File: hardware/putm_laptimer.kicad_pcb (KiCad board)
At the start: 4 copper layers, 76 x 75 mm, 48 parts, among them J1 Conn_01x22, J10 Conn_01x07, J11 Conn_01x09, J12 Conn_01x01, J13 Conn_01x01, J14 Conn_01x01, J15 Conn_01x01, J2 Conn_01x22, J3 Conn_01x22, J4 Conn_01x22, J5 M80-5001805, J6 Conn_02x05_Odd_Even, J7 734-163, J8 734-162, J9 Conn_01x07

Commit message: Increased buck converter pin hole diameter
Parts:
- J12, J13, J14, J15: footprint TestPoint:TestPoint_THTPad_D1.5mm_Drill0.7mm -> TestPoint:TestPoint_THTPad_D2.0mm_Drill1.0mm
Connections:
- net /IO13_GATE2 renamed /IO13
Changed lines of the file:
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@@
 	(net 18 "/IO19_PIN")
 	(net 19 "/IO14_GATE1")
-	(net 20 "/IO13_GATE2")
+	(net 20 "/IO13")
 	(net 21 "/IO37_PIN")
 	(net 22 "/IO35_PIN")
@@
 			(layers "*.Cu" "*.Mask")
 			(remove_unused_layers no)
-			(net 20 "/IO13_GATE2")
+			(net 20 "/IO13")
 			(pinfunction "Pin_19")
 			(pintype "passive")
@@
 		)
 	)
-	(footprint "TestPoint:TestPoint_THTPad_D1.5mm_Drill0.7mm"
+	(footprint "TestPoint:TestPoint_THTPad_D2.0mm_Drill1.0mm"
 		(layer "F.Cu")
 		(at 133.96 91.5 90)
-		(descr "THT pad as test Point, diameter 1.5mm, hole diameter 0.7mm")
+		(descr "THT pad as test Point, diameter 2.0mm, hole diameter 1.0mm")
 		(tags "test point THT pad")
 		(property "Reference" "J14"
-			(at 4 0.124695 90)
+			(at 3 0.04 180)
 			(layer "F.SilkS")
 			(effects
 				(font
-					(size 1 1)
+					(size 0.7 0.7)
 					(thickness 0.15)
 				)
@@
 		)
 		(property "Value" "Conn_01x01"
-			(at 0 1.75 90)
+			(at 0 2.05 90)
 			(layer "F.Fab")
 			(effects
@@
 		(fp_circle
 			(center 0 0)
-			(end 0 0.95)
+			(end 0 1.2)
 			(stroke
 				(width 0.12)
@@
 		(fp_circle
 			(center 0 0)
-			(end 1.25 0)
+			(end 1.5 0)
 			(stroke
 				(width 0.05)
@@
 		)
 		(fp_text user "${REFERENCE}"
-			(at 0 -1.65 90)
+			(at 0 -2 90)
 			(layer "F.Fab")
 			(effects
@@
 		(pad "1" thru_hole circle
 			(at 0 0 90)
-			(size 1.5 1.5)
-			(drill 0.7)
+			(size 2 2)
+			(drill 1)
 			(layers "*.Cu" "*.Mask")
 			(remove_unused_layers no)
@@
 		(embedded_fonts no)
 	)
-	(footprint "TestPoint:TestPoint_THTPad_D1.5mm_Drill0.7mm"
+	(footprint "TestPoint:TestPoint_THTPad_D2.0mm_Drill1.0mm"
 		(layer "F.Cu")
 		(at 136.5 91.5 90)
-		(descr "THT pad as test Point, diameter 1.5mm, hole diameter 0.7mm")
+		(descr "THT pad as test Point, diameter 2.0mm, hole diameter 1.0mm")
 		(tags "test point THT pad")
 		(property "Reference" "J15"
-			(at 4 0.084695 90)
+			(at 3 0 180)
 			(layer "F.SilkS")
 			(effects
 				(font
-					(size 1 1)
+					(size 0.7 0.7)
 					(thickness 0.15)
 				)
@@
 		)
 		(property "Value" "Conn_01x01"
-			(at 0 1.75 90)
+			(at 0 2.05 90)
 			(layer "F.Fab")
 			(effects
@@
 		(fp_circle
 			(center 0 0)
-			(end 0 0.95)
+			(end 0 1.2)
 			(stroke
 				(width 0.12)
@@
 		(fp_circle
 			(center 0 0)
-			(end 1.25 0)
+			(end 1.5 0)
 			(stroke
 				(width 0.05)
@@
 		)
 		(fp_text user "${REFERENCE}"
-			(at 0 -1.65 90)
+			(at 0 -2 90)
 			(layer "F.Fab")
 			(effects
@@
 		(pad "1" thru_hole circle
 			(at 0 0 90)
-			(size 1.5 1.5)
-			(drill 0.7)
+			(size 2 2)
+			(drill 1)
 			(layers "*.Cu" "*.Mask")
 			(remove_unused_layers no)
@@
 		)
 	)
-	(footprint "TestPoint:TestPoint_THTPad_D1.5mm_Drill0.7mm"
+	(footprint "TestPoint:TestPoint_THTPad_D2.0mm_Drill1.0mm"
 		(layer "F.Cu")
 		(at 128.88 91.5 90)
-		(descr "THT pad as test Point, diameter 1.5mm, hole diameter 0.7mm")
+		(descr "THT pad as test Point, diameter 2.0mm, hole diameter 1.0mm")
 		(tags "test point THT pad")
 		(property "Reference" "J12"
-			(at 4 0.08 90)
+			(at 3 0.06 180)
 			(layer "F.SilkS")
 			(effects
 				(font
-					(size 1 1)
+					(size 0.7 0.7)
 					(thickness 0.15)
 				)
@@
 		)
 		(property "Value" "Conn_01x01"
-			(at 0 1.75 90)
+			(at 0 2.05 90)
 			(layer "F.Fab")
 			(effects
@@
 		(fp_circle
 			(center 0 0)
-			(end 0 0.95)
+			(end 0 1.2)
 			(stroke
 				(width 0.12)
@@
 		(fp_circle
 			(center 0 0)
-			(end 1.25 0)
+			(end 1.5 0)
 			(stroke
 				(width 0.05)
@@
 		)
 		(fp_text user "${REFERENCE}"
-			(at 0 -1.65 90)
+			(at 0 -2 90)
 			(layer "F.Fab")
 			(effects
@@
 		(pad "1" thru_hole circle
 			(at 0 0 90)
-			(size 1.5 1.5)
-			(drill 0.7)
+			(size 2 2)
+			(drill 1)
 			(layers "*.Cu" "*.Mask")
 			(remove_unused_layers no)
@@
 			(layers "*.Cu" "*.Mask")
 			(remove_unused_layers no)
-			(net 20 "/IO13_GATE2")
+			(net 20 "/IO13")
 			(pinfunction "Pin_19")
 			(pintype "passive")
@@
 			)
 		)
-		(property "Datasheet" "734-162"
+		(property "Datasheet" "https://www.wago.com/pl/wielowtyki/wtyk-tht/p/734-162#details"
 			(at 0 0 0)
 			(layer "F.Fab")
@@
 		)
 	)
-	(footprint "TestPoint:TestPoint_THTPad_D1.5mm_Drill0.7mm"
+	(footprint "TestPoint:TestPoint_THTPad_D2.0mm_Drill1.0mm"
 		(layer "F.Cu")
 		(at 131.42 91.5 90)
-		(descr "THT pad as test Point, diameter 1.5mm, hole diameter 0.7mm")
+		(descr "THT pad as test Point, diameter 2.0mm, hole diameter 1.0mm")
 		(tags "test point THT pad")
 		(property "Reference" "J13"
-			(at 4 0 90)
+			(at 3 0.08 180)
 			(layer "F.SilkS")
 			(effects
 				(font
-					(size 1 1)
+					(size 0.7 0.7)
 					(thickness 0.15)
 				)
@@
 		)
 		(property "Value" "Conn_01x01"
-			(at 0 1.75 90)
+			(at 0 2.05 90)
 			(layer "F.Fab")
 			(effects
@@
 		(fp_circle
 			(center 0 0)
-			(end 0 0.95)
+			(end 0 1.2)
 			(stroke
 				(width 0.12)
@@
 		(fp_circle
 			(center 0 0)
-			(end 1.25 0)
+			(end 1.5 0)
 			(stroke
 				(width 0.05)
@@
 		)
 		(fp_text user "${REFERENCE}"
-			(at 0 -1.65 90)
+			(at 0 -2 90)
 			(layer "F.Fab")
 			(effects
@@
 		(pad "1" thru_hole circle
 			(at 0 0 90)
-			(size 1.5 1.5)
-			(drill 0.7)
+			(size 2 2)
+			(drill 1)
 			(layers "*.Cu" "*.Mask")
 			(remove_unused_layers no)
@@
 			)
 		)
-		(property "Datasheet" "734-163"
+		(property "Datasheet" "https://www.wago.com/pl/wielowtyki/wtyk-tht/p/734-163#details"
 			(at 0 0 0)
 			(layer "F.Fab")

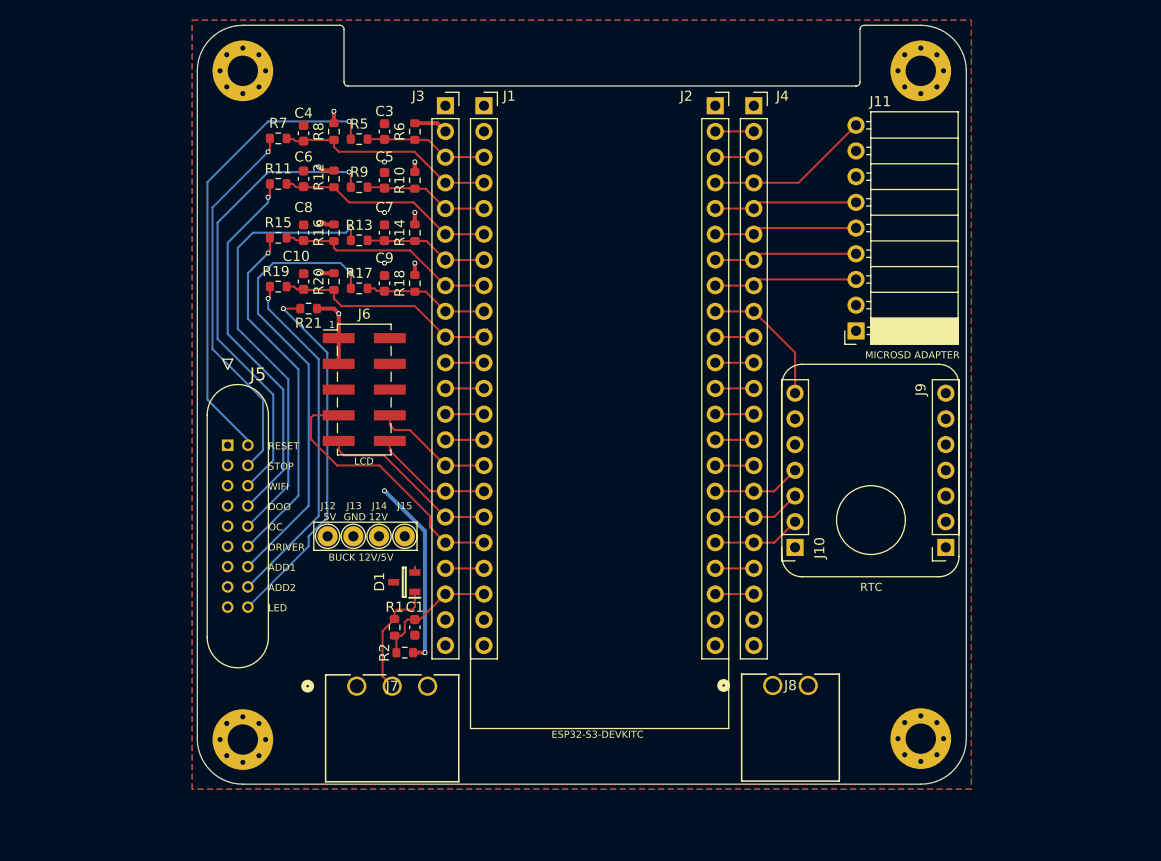
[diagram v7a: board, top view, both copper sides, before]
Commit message: Changed connectors
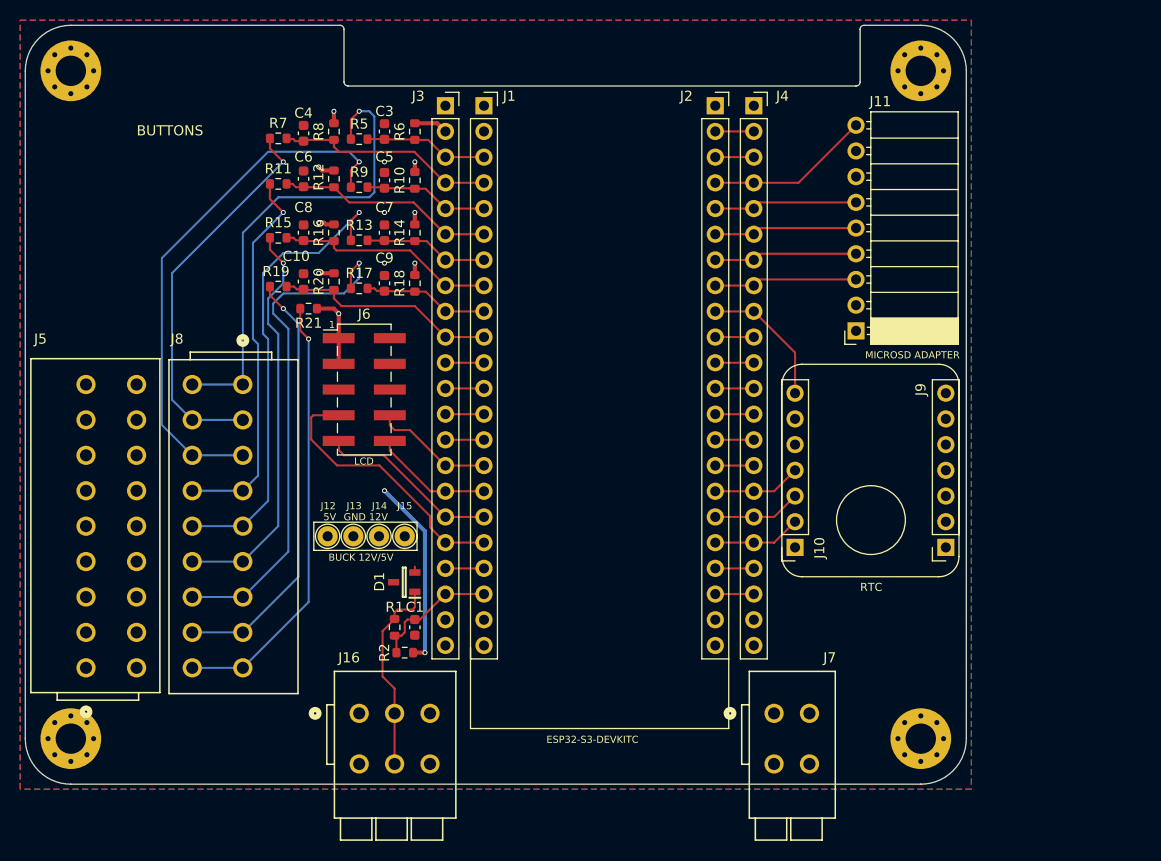
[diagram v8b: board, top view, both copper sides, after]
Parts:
- added J16: 2601-1103, Footprint:CONN3_2601-1103_WAG, F.Cu at (132.0, 109.0)
- J5: value M80-5001805 -> 2601-3109; footprint Footprint:M80-50018YY_2 -> Footprint:CONN9_2601-3109_WAG
- J7: value 734-163 -> 2601-1102; footprint Footprint:CONN3_734-163_WAG -> Footprint:CONN2_2601-1102_WAG
- J8: value 734-162 -> 2601-3109; footprint Footprint:CONN2_734-162_WAG -> Footprint:CONN9_2601-3109_WAG
- moved J8 60.2 mm to (120.5, 76.5), turned to -90 degrees
- moved J7 41.3 mm to (173.0, 109.0)
- moved J5 26.1 mm to (105.0, 104.5), turned to 90 degrees
- moved REF** 17.0 mm to (103.5, 111.5)
- moved REF** 17.0 mm to (103.5, 45.5)
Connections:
- D1 pad 1: Net-(D1-Pad1) -> Net-(J16-2_1)
- J5 pad 10: /RST_BTN -> GND
- J5 pad 11: /STOP_BTN -> GND
- J5 pad 12: /WIFI_BTN -> GND
- J5 pad 13: /DOO_BTN -> GND
- J5 pad 14: /OC_BTN -> GND
- J5 pad 15: /DRIVER_BTN -> GND
- J5 pad 16: /ADD1_BTN -> GND
- J5 pad 17: /ADD2_BTN -> GND
- J5 pad 18: /PWR_LED -> GND
- J7 pad 2: Net-(D1-Pad1) -> +12V
- J8 pad 1: +12V -> /RST_BTN
- J8 pad 2: GND -> /RST_BTN
- R1 pad 2: Net-(D1-Pad1) -> Net-(J16-2_1)
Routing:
- net Net-(J16-2_1): track 0.00 -> 19.7 mm
- net Net-(D1-Pad1): track 11.9 -> 0.00 mm
- net /ADD2_BTN: track 34.7 -> 42.6 mm
- net /PWR_LED: track 36.2 -> 43.5 mm
- net /WIFI_BTN: track 46.0 -> 52.8 mm
- net /ADD1_BTN: track 45.1 -> 50.4 mm
- net /DRIVER_BTN: track 35.5 -> 40.0 mm
- net /OC_BTN: track 44.5 -> 46.3 mm
- net /STOP_BTN: track 37.4 -> 38.8 mm
- net /RST_BTN: track 46.0 -> 47.0 mm
- net /DOO_BTN: track 37.3 -> 37.9 mm
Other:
- board size 76 x 75 mm -> 93 x 75 mm
- board text added: "BUTTONS"
- board text removed: "ADD1"
- board text removed: "ADD2"
- board text removed: "DOO"
- board text removed: "DRIVER"
- board text removed: "LCD MODULE"
- board text removed: "LED"
- board text removed: "OC"
- board text removed: "RESET"
- board text removed: "STOP"
- board text removed: "WIFI"
